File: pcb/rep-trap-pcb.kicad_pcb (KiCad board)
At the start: 4 copper layers, 154.2 x 30 mm, 77 parts, among them IC1 DRV5032FB, J3 SJ-3541AS-SMT-TR-67, J4 +5V, J5 Conn_01x02_Pin, J7 GND, J8 124018612112A, J9 DNP, SW1 SKRKAEE020, SW2 SKRKAEE020, U1 AP2112K-3.3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

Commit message: Removed diode from VBUS to 5V+ and removed 5V+ because it is not needed
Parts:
- removed D7: 1N5819HW-7-F, 1N5819HW-7-F:SOD3716X145N
- J4: value +5V -> VBUS
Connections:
- C3 pad 1: +5V -> VBUS
- D2 pad 2: +5V -> VBUS
- J4 pad 1: +5V -> VBUS
- R2 pad 1: +5V -> VBUS
- U2 pad 4: +5V -> VBUS
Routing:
- net +5V: track 142.8 -> 0.00 mm, vias 9 -> 0
- net VBUS: track 12.3 -> 147.2 mm, vias 7 -> 17
- added copper zone on F.Cu, net VBUS
- removed copper zone on F.Cu, net +5V
- removed copper zone on In2.Cu, net +5V

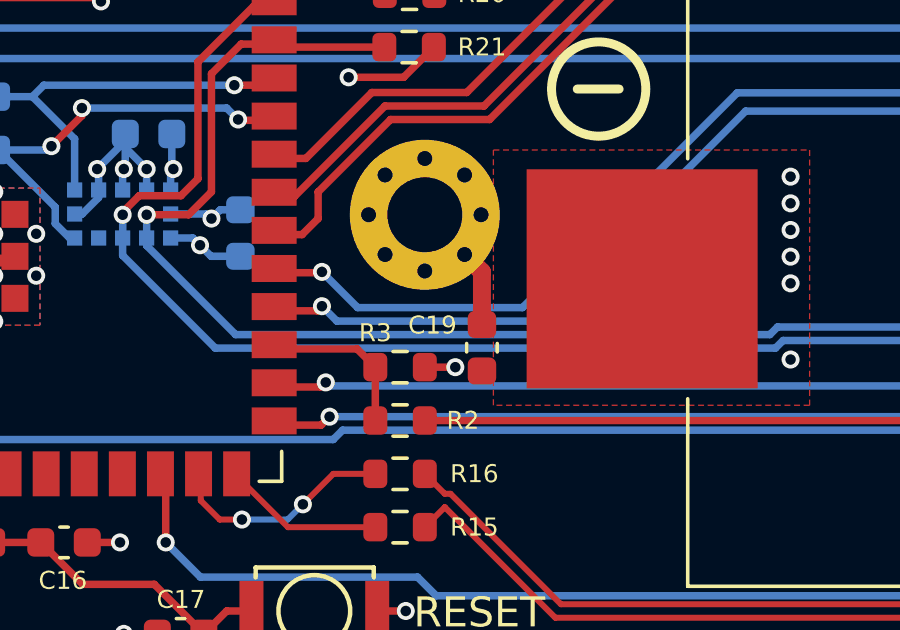
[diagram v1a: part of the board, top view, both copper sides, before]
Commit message: Removed capacitor from one of the mountingholes
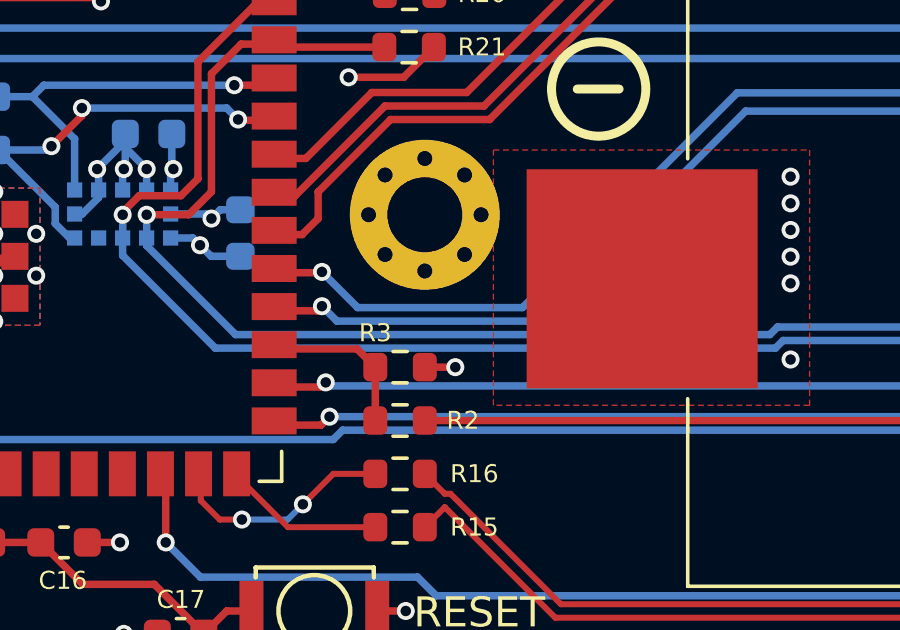
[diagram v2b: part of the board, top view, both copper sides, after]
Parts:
- removed C19: 0.1µF, Capacitor_SMD:C_0603_1608Metric
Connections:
- H2 pad 1: Net-(C19-Pad1) -> unconnected-(H2-Pad1)
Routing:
- net Net-(C19-Pad1): track 2.57 -> 0.00 mm
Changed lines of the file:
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@@
   (net 77 "unconnected-(U7-GPIO1{slash}TOUCH1{slash}ADC1_CH0-Pad39)")
   (net 78 "unconnected-(U7-GPIO4{slash}TOUCH4{slash}ADC1_CH3-Pad4)")
-  (net 79 "Net-(C19-Pad1)")
+  (net 79 "unconnected-(H2-Pad1)")
   (net 80 "Net-(C20-Pad1)")
   (footprint "Resistor_SMD:R_0603_1608Metric" (layer "F.Cu")
@@
       (stroke (width 0.05) (type solid)) (fill none) (layer "F.CrtYd"))
     (pad "1" thru_hole circle (at -1.875 0) (size 0.8 0.8) (drill 0.5) (layers "*.Cu" "*.Mask")
-      (net 79 "Net-(C19-Pad1)") (pinfunction "1") (pintype "input"))
+      (net 79 "unconnected-(H2-Pad1)") (pinfunction "1") (pintype "input+no_connect"))
     (pad "1" thru_hole circle (at -1.325825 -1.325825) (size 0.8 0.8) (drill 0.5) (layers "*.Cu" "*.Mask")
-      (net 79 "Net-(C19-Pad1)") (pinfunction "1") (pintype "input"))
+      (net 79 "unconnected-(H2-Pad1)") (pinfunction "1") (pintype "input+no_connect"))
     (pad "1" thru_hole circle (at -1.325825 1.325825) (size 0.8 0.8) (drill 0.5) (layers "*.Cu" "*.Mask")
-      (net 79 "Net-(C19-Pad1)") (pinfunction "1") (pintype "input"))
+      (net 79 "unconnected-(H2-Pad1)") (pinfunction "1") (pintype "input+no_connect"))
     (pad "1" thru_hole circle (at 0 -1.875) (size 0.8 0.8) (drill 0.5) (layers "*.Cu" "*.Mask")
-      (net 79 "Net-(C19-Pad1)") (pinfunction "1") (pintype "input"))
+      (net 79 "unconnected-(H2-Pad1)") (pinfunction "1") (pintype "input+no_connect"))
     (pad "1" thru_hole circle (at 0 0) (size 5 5) (drill 2.5) (layers "*.Cu" "*.Mask")
-      (net 79 "Net-(C19-Pad1)") (pinfunction "1") (pintype "input"))
+      (net 79 "unconnected-(H2-Pad1)") (pinfunction "1") (pintype "input+no_connect"))
     (pad "1" thru_hole circle (at 0 1.875) (size 0.8 0.8) (drill 0.5) (layers "*.Cu" "*.Mask")
-      (net 79 "Net-(C19-Pad1)") (pinfunction "1") (pintype "input"))
+      (net 79 "unconnected-(H2-Pad1)") (pinfunction "1") (pintype "input+no_connect"))
     (pad "1" thru_hole circle (at 1.325825 -1.325825) (size 0.8 0.8) (drill 0.5) (layers "*.Cu" "*.Mask")
-      (net 79 "Net-(C19-Pad1)") (pinfunction "1") (pintype "input"))
+      (net 79 "unconnected-(H2-Pad1)") (pinfunction "1") (pintype "input+no_connect"))
     (pad "1" thru_hole circle (at 1.325825 1.325825) (size 0.8 0.8) (drill 0.5) (layers "*.Cu" "*.Mask")
-      (net 79 "Net-(C19-Pad1)") (pinfunction "1") (pintype "input"))
+      (net 79 "unconnected-(H2-Pad1)") (pinfunction "1") (pintype "input+no_connect"))
     (pad "1" thru_hole circle (at 1.875 0) (size 0.8 0.8) (drill 0.5) (layers "*.Cu" "*.Mask")
-      (net 79 "Net-(C19-Pad1)") (pinfunction "1") (pintype "input"))
+      (net 79 "unconnected-(H2-Pad1)") (pinfunction "1") (pintype "input+no_connect"))
   )
   (footprint "SKRKAEE020:SKRKAEE020" (layer "F.Cu")
@@
       (net 80 "Net-(C20-Pad1)") (pinfunction "1") (pintype "input"))
   )
-  (footprint "Capacitor_SMD:C_0603_1608Metric" (layer "F.Cu")
-    (at 101.346 98.666 -90)
-    (descr "Capacitor SMD 0603 (1608 Metric), square (rectangular) end terminal, IPC_7351 nominal, (Body size source: IPC-SM-782 page 76, https://www.pcb-3d.com/wordpress/wp-content/uploads/ipc-sm-782a_amendment_1_and_2.pdf), generated with kicad-footprint-generator")
-    (tags "capacitor")
-    (property "Sheetfile" "main.kicad_sch")
-    (property "Sheetname" "main")
-    (property "ki_description" "Unpolarized capacitor")
-    (property "ki_keywords" "cap capacitor")
-    (attr smd)
-    (fp_text reference "C19" (at -0.749 1.651 -180) (layer "F.SilkS")
-        (effects (font (size 0.6 0.6) (thickness 0.15)))
-    )
-    (fp_text value "0.1µF" (at 0 1.43 90) (layer "F.Fab")
-        (effects (font (size 1 1) (thickness 0.15)))
-    )
-    (fp_text user "${REFERENCE}" (at 0 0 90) (layer "F.Fab")
-        (effects (font (size 0.4 0.4) (thickness 0.06)))
-    )
-    (fp_line (start -0.14058 -0.51) (end 0.14058 -0.51)
-      (stroke (width 0.12) (type solid)) (layer "F.SilkS"))
-    (fp_line (start -0.14058 0.51) (end 0.14058 0.51)
-      (stroke (width 0.12) (type solid)) (layer "F.SilkS"))
-    (fp_line (start -1.48 -0.73) (end 1.48 -0.73)
-      (stroke (width 0.05) (type solid)) (layer "F.CrtYd"))
-    (fp_line (start -1.48 0.73) (end -1.48 -0.73)
-      (stroke (width 0.05) (type solid)) (layer "F.CrtYd"))
-    (fp_line (start 1.48 -0.73) (end 1.48 0.73)
-      (stroke (width 0.05) (type solid)) (layer "F.CrtYd"))
-    (fp_line (start 1.48 0.73) (end -1.48 0.73)
-      (stroke (width 0.05) (type solid)) (layer "F.CrtYd"))
-    (fp_line (start -0.8 -0.4) (end 0.8 -0.4)
-      (stroke (width 0.1) (type solid)) (layer "F.Fab"))
-    (fp_line (start -0.8 0.4) (end -0.8 -0.4)
-      (stroke (width 0.1) (type solid)) (layer "F.Fab"))
-    (fp_line (start 0.8 -0.4) (end 0.8 0.4)
-      (stroke (width 0.1) (type solid)) (layer "F.Fab"))
-    (fp_line (start 0.8 0.4) (end -0.8 0.4)
-      (stroke (width 0.1) (type solid)) (layer "F.Fab"))
-    (pad "1" smd roundrect (at -0.775 0 270) (size 0.9 0.95) (layers "F.Cu" "F.Paste" "F.Mask") (roundrect_rratio 0.25)
-      (net 79 "Net-(C19-Pad1)") (pintype "passive"))
-    (pad "2" smd roundrect (at 0.775 0 270) (size 0.9 0.95) (layers "F.Cu" "F.Paste" "F.Mask") (roundrect_rratio 0.25)
-      (net 2 "GND") (pintype "passive"))
-    (model "${KICAD6_3DMODEL_DIR}/Capacitor_SMD.3dshapes/C_0603_1608Metric.wrl"
-      (offset (xyz 0 0 0))
-      (scale (xyz 1 1 1))
-      (rotate (xyz 0 0 0))
-    )
-  )
   (footprint "Resistor_SMD:R_0603_1608Metric" (layer "F.Cu")
     (at 196.406 80.645 180)
@@
   (segment (start 212.725 80.772) (end 212.06 81.437) (width 0.4) (layer "F.Cu") (net 75))
   (segment (start 212.06 81.437) (end 209.55 81.437) (width 0.4) (layer "F.Cu") (net 75))
-  (segment (start 101.346 96.139) (end 100.766825 95.559825) (width 0.6) (layer "F.Cu") (net 79))
-  (segment (start 101.346 97.891) (end 101.346 96.139) (width 0.6) (layer "F.Cu") (net 79))
   (segment (start 218.922 94.208) (end 218.948 94.234) (width 0.6) (layer "F.Cu") (net 80))
   (segment (start 214.884 94.208) (end 218.922 94.208) (width 0.6) (layer "F.Cu") (net 80))

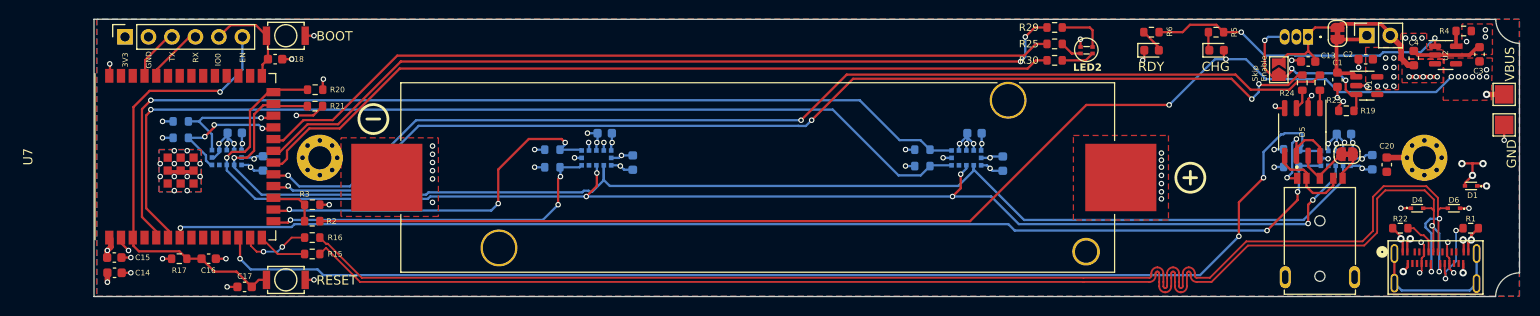
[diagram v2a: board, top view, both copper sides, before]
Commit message: Changed net names to match functionallity of active low
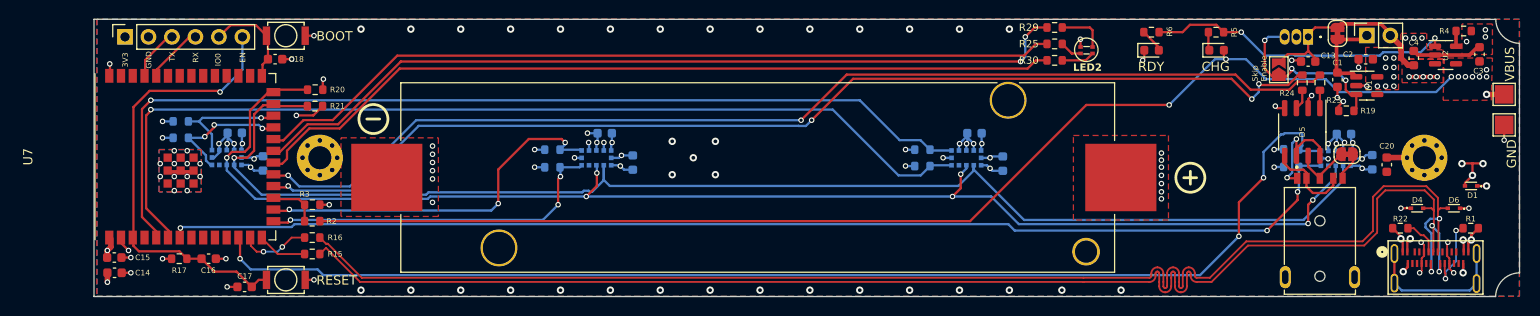
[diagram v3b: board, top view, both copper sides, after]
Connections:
- net /main/MCU/INT_VL53_1 renamed /main/MCU/~{INT_VL53_1}
- net /main/MCU/INT_VL53_2 renamed /main/MCU/~{INT_VL53_2}
- net /main/MCU/INT_VL53_3 renamed /main/MCU/~{INT_VL53_3}
- net /main/MCU/INT_VL53_4 renamed /main/MCU/~{INT_VL53_4}
- net /main/MCU/XSHUT_VL53_1 renamed /main/MCU/~{XSHUT_VL53_1}
- net /main/MCU/XSHUT_VL53_2 renamed /main/MCU/~{XSHUT_VL53_2}
- net /main/MCU/XSHUT_VL53_3 renamed /main/MCU/~{XSHUT_VL53_3}
- net /main/MCU/XSHUT_VL53_4 renamed /main/MCU/~{XSHUT_VL53_4}
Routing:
- net GND: vias 71 -> 106

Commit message: Moved magnet switch to the other side
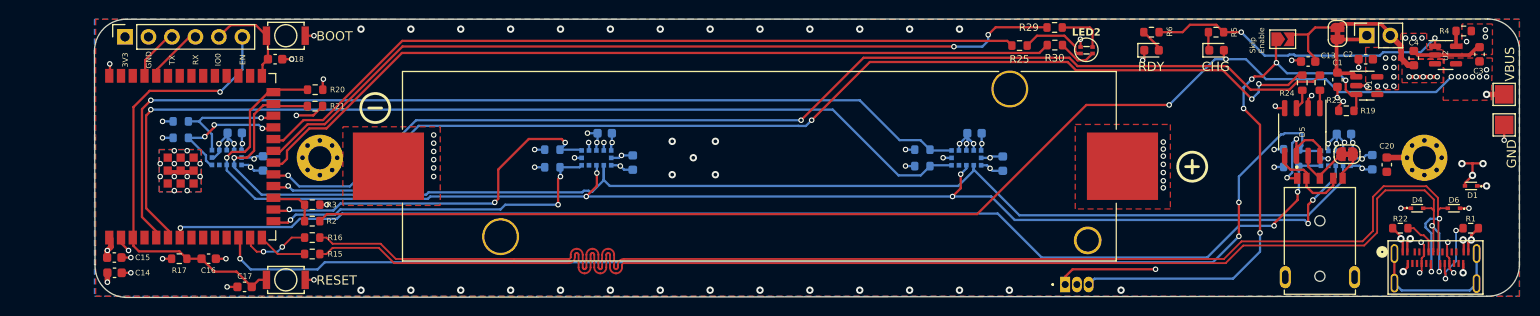
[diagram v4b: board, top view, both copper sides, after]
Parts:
- C14: value 10uF -> 10µF
- C15: value 0.1uF -> 0.1µF
- C16: value 1uF -> 1µF
- C17, C18: value 0.1uF/DNP -> 0.1µF/DNP
- moved IC1 37.5 mm to (180.1, 108.0), turned to 180 degrees
- moved R25 3.80 mm to (175.1, 82.1)
- moved JP1 3.33 mm to (203.6, 81.4), turned to 0 degrees
- moved R30 1.65 mm to (179.0, 82.0)
- moved BT1 1.23 mm to (146.9, 95.1)
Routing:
- net /main/ENABLE: track 19.8 -> 58.3 mm, vias 3 -> 5
- net +BATT: track 24.4 -> 43.3 mm, vias 12 -> 13
- net Net-(LED2-R): track 2.41 -> 7.32 mm
- net /main/MCU/~{INT_VL53_4}: track 130.0 -> 133.5 mm
- net /main/MCU/LED_R: track 88.0 -> 84.5 mm
- net /main/SHUTTER: track 120.0 -> 121.5 mm
- net /main/AUTOFOCUS: track 119.2 -> 120.7 mm
- net /main/MCU/LED_G: track 90.5 -> 89.6 mm
- net /main/MCU/LED_B: track 88.8 -> 89.5 mm
- net Net-(LED2-B): track 3.59 -> 4.25 mm
- net GND: track 83.7 -> 84.3 mm, vias 106 -> 104
- net /main/MCU/~{XSHUT_VL53_4}: track 132.3 -> 131.8 mm
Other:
- board size 154.2 x 30 mm -> 154.2 x 30.1 mm

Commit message: Updated footprints try to fix DRC
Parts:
- R29: value 2k2 -> 2.2k
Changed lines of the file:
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@@
     (property "Sheetfile" "mcu.kicad_sch")
     (property "Sheetname" "MCU")
+    (property "exclude_from_bom" "")
     (property "ki_description" "Generic connector, single row, 01x06, script generated")
     (property "ki_keywords" "connector")
@@
     (property "Sheetfile" "psu_charging.kicad_sch")
     (property "Sheetname" "PSU and charging")
+    (property "exclude_from_bom" "")
     (property "ki_description" "Jumper, 2-pole, closed/bridged")
     (property "ki_keywords" "Jumper SPST")
@@
     (property "Sheetfile" "main.kicad_sch")
     (property "Sheetname" "main")
+    (property "exclude_from_bom" "")
     (property "ki_description" "Mounting Hole with connection")
     (property "ki_keywords" "mounting hole")
@@
     (property "Sheetfile" "psu_charging.kicad_sch")
     (property "Sheetname" "PSU and charging")
+    (property "exclude_from_bom" "")
     (property "ki_description" "Generic connector, single row, 01x02, script generated")
     (property "ki_keywords" "connector")
@@
     (property "Sheetfile" "main.kicad_sch")
     (property "Sheetname" "main")
+    (property "exclude_from_bom" "")
     (property "ki_description" "Mounting Hole with connection")
     (property "ki_keywords" "mounting hole")
@@
         (effects (font (size 0.8 0.8) (thickness 0.15)))
     )
-    (fp_text value "2k2" (at 0 1.43) (layer "F.Fab")
-        (effects (font (size 1 1) (thickness 0.15)))
-    )
+    (fp_text value "2.2k" (at 0 1.43) (layer "F.Fab")
+        (effects (font (size 1 1) (thickness 0.15)))
+    )

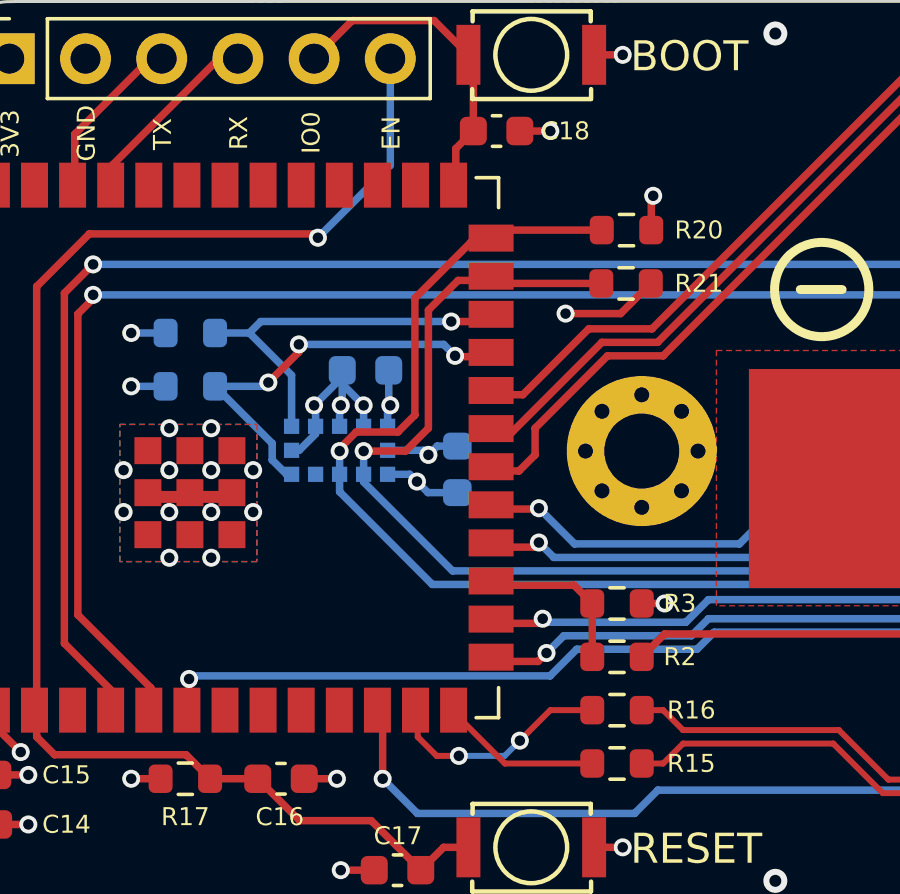
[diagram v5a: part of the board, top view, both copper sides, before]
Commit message: Fixed usage of strapping pins
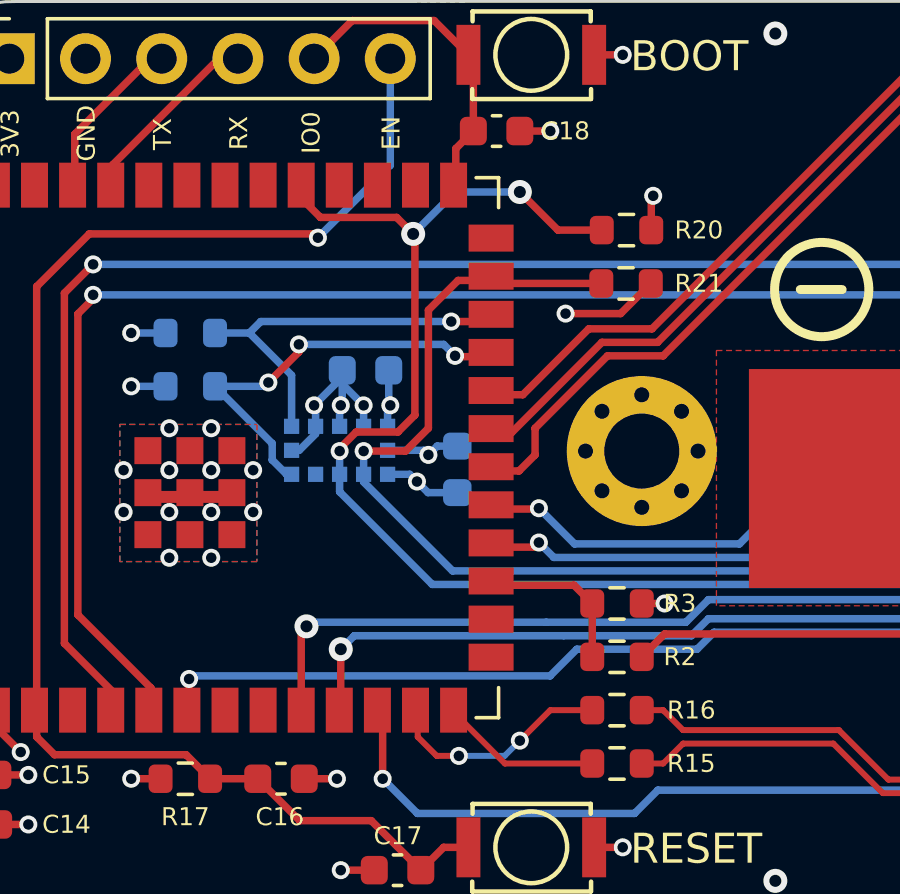
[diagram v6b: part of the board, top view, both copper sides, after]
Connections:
- U7 pad 10: unconnected-(U7-GPIO17/U1TXD/ADC2_CH6-Pad10) -> /main/MCU/~{XSHUT_VL53_2}
- U7 pad 11: unconnected-(U7-GPIO18/U1RXD/ADC2_CH7/CLK_OUT3-Pad11) -> /main/MCU/~{INT_VL53_2}
- U7 pad 15: /main/MCU/~{INT_VL53_2} -> unconnected-(U7-GPIO3/TOUCH3/ADC1_CH2-Pad15)
- U7 pad 16: /main/MCU/~{XSHUT_VL53_2} -> unconnected-(U7-GPIO46-Pad16)
- U7 pad 26: /main/MCU/SDA -> unconnected-(U7-GPIO45-Pad26)
- U7 pad 31: unconnected-(U7-GPIO38/FSPIWP/SUBSPIWP-Pad31) -> /main/MCU/SDA
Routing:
- net /main/MCU/~{XSHUT_VL53_2}: track 40.2 -> 49.2 mm
- net /main/MCU/SDA: track 150.4 -> 157.5 mm, vias 7 -> 9
- net /main/MCU/~{INT_VL53_2}: track 38.1 -> 45.1 mm

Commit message: Updated PCB with changed values
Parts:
- IC1: value DRV5032FB -> DRV5032FBLPG
- R19: value 10k -> 10k/DNP
- R23, R24: value 100R -> 47R
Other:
- board text added: "Rep Trap - REV-B Prototype"
- board text removed: "Rep Trap - Rev0.2 Prototype"
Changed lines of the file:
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@@
         (effects (font (size 0.6 0.6) (thickness 0.15)))
     )
-    (fp_text value "100R" (at 0 1.43 90) (layer "F.Fab")
+    (fp_text value "47R" (at 0 1.43 90) (layer "F.Fab")
         (effects (font (size 1 1) (thickness 0.15)))
     )
@@
         (effects (font (size 0.6 0.6) (thickness 0.15)))
     )
-    (fp_text value "100R" (at 0 1.43 90) (layer "F.Fab")
+    (fp_text value "47R" (at 0 1.43 90) (layer "F.Fab")
         (effects (font (size 1 1) (thickness 0.15)))
     )
@@
         (effects (font (size 0.6 0.6) (thickness 0.15)))
     )
-    (fp_text value "10k" (at 0 1.43) (layer "F.Fab")
+    (fp_text value "10k/DNP" (at 0 1.43) (layer "F.Fab")
         (effects (font (size 1 1) (thickness 0.15)))
     )
@@
         (effects (font (size 1.27 1.27) (thickness 0.254)))
     )
-    (fp_text value "DRV5032FB" (at -1.27 -0.064) (layer "F.SilkS") hide
+    (fp_text value "DRV5032FBLPG" (at -1.27 -0.064) (layer "F.SilkS") hide
         (effects (font (size 1.27 1.27) (thickness 0.254)))
     )
@@
     (effects (font (size 1.5 1.5) (thickness 0.3) bold) (justify left bottom mirror))
   )
-  (gr_text "Rep Trap - Rev0.2 Prototype" (at 159.258 107.569) (layer "B.SilkS")
+  (gr_text "Rep Trap - REV-B Prototype" (at 159.258 107.569) (layer "B.SilkS")
     (effects (font (size 1 1) (thickness 0.15)) (justify left bottom mirror))
   )
